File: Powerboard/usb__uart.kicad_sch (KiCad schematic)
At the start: 27 parts

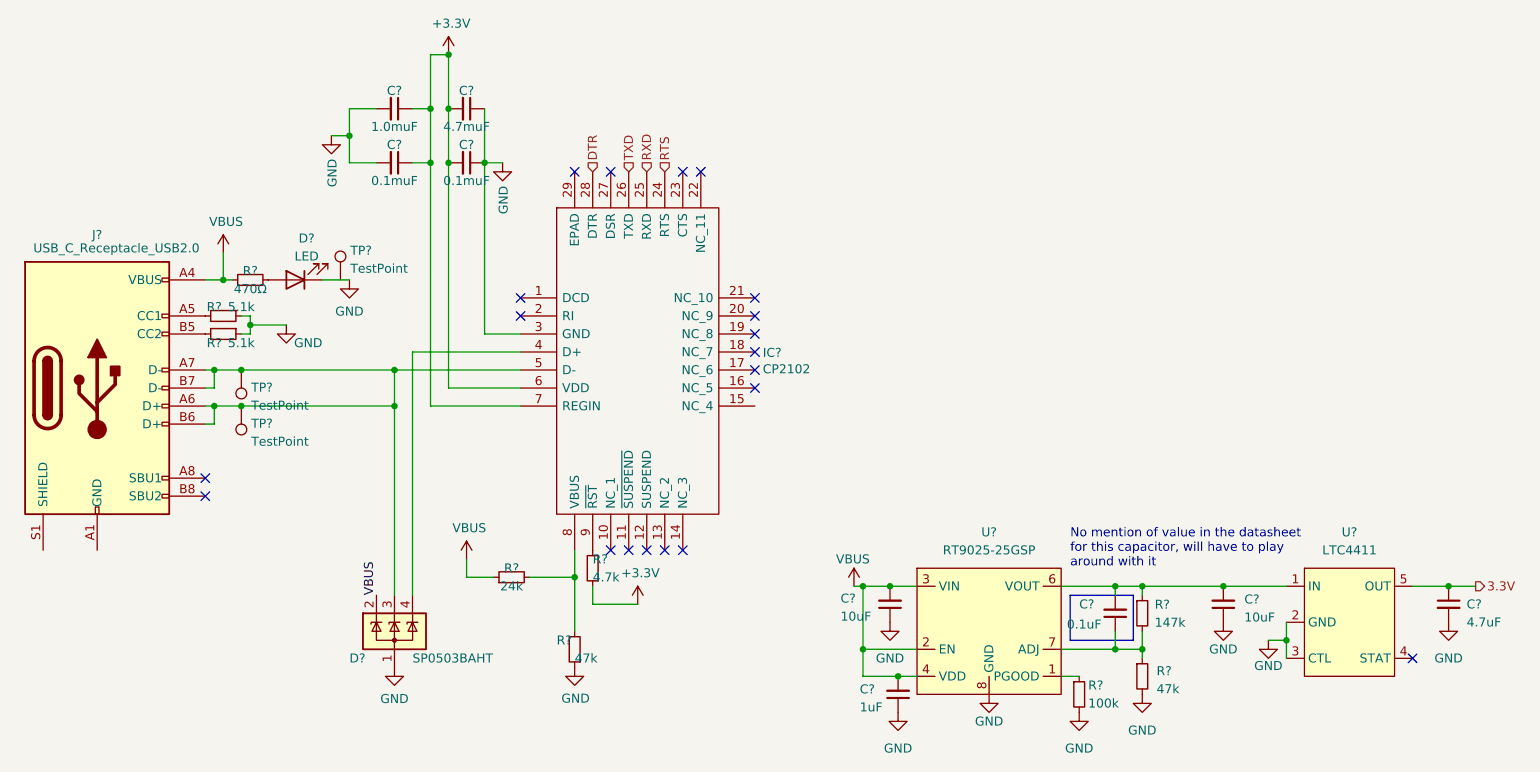
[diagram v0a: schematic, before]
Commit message: removed charger reverse polarity protection
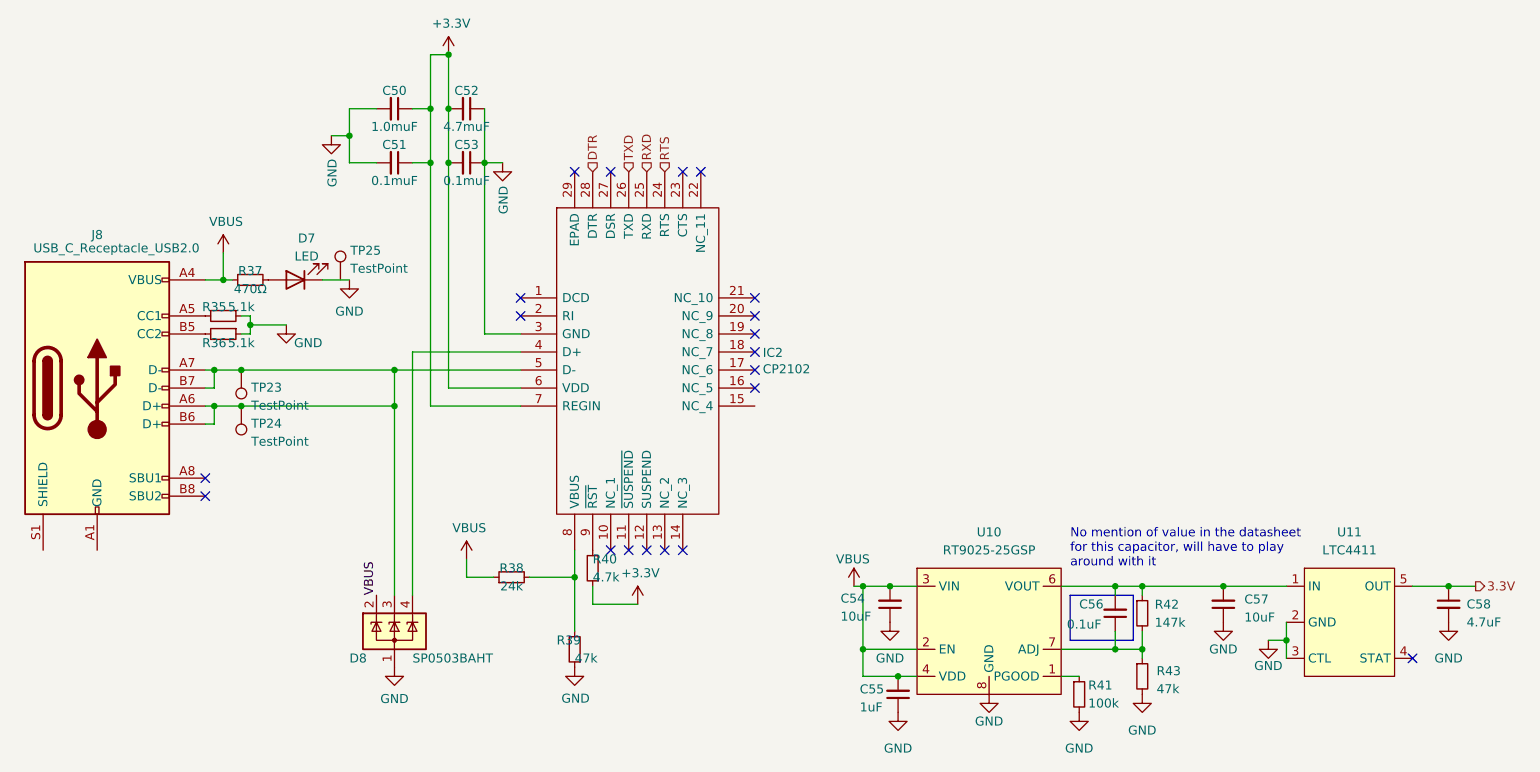
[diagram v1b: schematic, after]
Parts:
- gave numbers to parts that had none: 27

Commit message: changed old mosfets, broke out I2C
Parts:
- removed C55: 1uF, Capacitor_SMD:C_0603_1608Metric, symbol Device:C_Small
- removed C56: 0.1uF, Capacitor_SMD:C_0603_1608Metric, symbol Device:C_Small
- removed R41: 100k, Resistor_SMD:R_0603_1608Metric, symbol Device:R_Small
- R42: value 147k -> 56k
- R43: value 47k -> 10k
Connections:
- net VBUS: no longer U10.4 (VDD)
- no-connect marks 20 -> 22
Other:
- note removed: "No mention of value in the datasheet for this capacitor, will have to play around with it"
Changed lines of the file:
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@@
   (junction (at 100.33 91.44) (diameter 0) (color 0 0 0 0)
   )
-  (junction (at 223.52 121.92) (diameter 0) (color 0 0 0 0)
-  )
   (junction (at 115.57 58.42) (diameter 0) (color 0 0 0 0)
   )
@@
   (junction (at 100.33 96.52) (diameter 0) (color 0 0 0 0)
   )
-  (junction (at 187.96 130.81) (diameter 0) (color 0 0 0 0)
-  )
   (junction (at 191.77 121.92) (diameter 0) (color 0 0 0 0)
   )
@@
   (junction (at 121.92 96.52) (diameter 0) (color 0 0 0 0)
   )
-  (junction (at 192.9078 134.62) (diameter 0) (color 0 0 0 0)
-  )
   (junction (at 134.62 62.23) (diameter 0) (color 0 0 0 0)
-  )
-  (junction (at 223.52 130.81) (diameter 0) (color 0 0 0 0)
   )
   (junction (at 127 62.23) (diameter 0) (color 0 0 0 0)
@@
   (no_connect (at 147.32 63.5))
   (no_connect (at 95.25 106.68))
+  (no_connect (at 215.9 134.62))
   (no_connect (at 162.56 63.5))
   (no_connect (at 172.72 88.9))
   (no_connect (at 157.48 116.84))
   (no_connect (at 160.02 116.84))
+  (no_connect (at 195.58 134.62))
   (no_connect (at 152.4 116.84))
   (no_connect (at 172.72 93.98))
@@
     (stroke (width 0) (type default) (color 0 0 0 0))
   )
-  (polyline (pts (xy 217.17 129.54) (xy 226.06 129.54))
-    (stroke (width 0) (type default) (color 0 0 0 0))
-  )
   (wire (pts (xy 191.77 121.92) (xy 195.58 121.92))
     (stroke (width 0) (type default) (color 0 0 0 0))
@@
     (stroke (width 0) (type default) (color 0 0 0 0))
   )
-  (polyline (pts (xy 226.06 129.54) (xy 226.06 123.19))
-    (stroke (width 0) (type default) (color 0 0 0 0))
-  )
   (wire (pts (xy 127 46.99) (xy 129.54 46.99))
     (stroke (width 0) (type default) (color 0 0 0 0))
@@
     (stroke (width 0) (type default) (color 0 0 0 0))
   )
-  (wire (pts (xy 223.52 130.81) (xy 227.33 130.81))
+  (wire (pts (xy 215.9 130.81) (xy 227.33 130.81))
     (stroke (width 0) (type default) (color 0 0 0 0))
   )
@@
     (stroke (width 0) (type default) (color 0 0 0 0))
   )
-  (wire (pts (xy 187.96 130.81) (xy 187.96 134.62))
-    (stroke (width 0) (type default) (color 0 0 0 0))
-  )
   (wire (pts (xy 227.33 128.27) (xy 227.33 130.81))
     (stroke (width 0) (type default) (color 0 0 0 0))
@@
     (stroke (width 0) (type default) (color 0 0 0 0))
   )
-  (polyline (pts (xy 217.17 123.19) (xy 217.17 129.54))
-    (stroke (width 0) (type default) (color 0 0 0 0))
-  )
   (wire (pts (xy 96.52 96.52) (xy 96.52 99.06))
     (stroke (width 0) (type default) (color 0 0 0 0))
@@
     (stroke (width 0) (type default) (color 0 0 0 0))
   )
-  (wire (pts (xy 187.96 134.62) (xy 192.9078 134.62))
-    (stroke (width 0) (type default) (color 0 0 0 0))
-  )
   (wire (pts (xy 147.32 120.65) (xy 147.32 128.27))
     (stroke (width 0) (type default) (color 0 0 0 0))
@@
     (stroke (width 0) (type default) (color 0 0 0 0))
   )
-  (wire (pts (xy 223.52 121.92) (xy 227.33 121.92))
+  (wire (pts (xy 215.9 121.92) (xy 227.33 121.92))
     (stroke (width 0) (type default) (color 0 0 0 0))
   )
@@
     (stroke (width 0) (type default) (color 0 0 0 0))
   )
-  (wire (pts (xy 192.9078 134.62) (xy 195.58 134.62))
-    (stroke (width 0) (type default) (color 0 0 0 0))
-  )
   (wire (pts (xy 95.25 96.52) (xy 96.52 96.52))
     (stroke (width 0) (type default) (color 0 0 0 0))
   )
-  (wire (pts (xy 215.9 130.81) (xy 223.52 130.81))
-    (stroke (width 0) (type default) (color 0 0 0 0))
-  )
   (wire (pts (xy 121.92 91.44) (xy 139.7 91.44))
     (stroke (width 0) (type default) (color 0 0 0 0))
   )
-  (wire (pts (xy 223.52 128.27) (xy 223.52 130.81))
-    (stroke (width 0) (type default) (color 0 0 0 0))
-  )
   (wire (pts (xy 115.57 58.42) (xy 115.57 62.23))
     (stroke (width 0) (type default) (color 0 0 0 0))
   )
-  (wire (pts (xy 215.9 134.62) (xy 218.44 134.62))
-    (stroke (width 0) (type default) (color 0 0 0 0))
-  )
   (wire (pts (xy 149.86 121.92) (xy 149.86 124.46))
     (stroke (width 0) (type default) (color 0 0 0 0))
   )
-  (wire (pts (xy 215.9 121.92) (xy 223.52 121.92))
-    (stroke (width 0) (type default) (color 0 0 0 0))
-  )
   (wire (pts (xy 97.79 74.93) (xy 97.79 78.74))
     (stroke (width 0) (type default) (color 0 0 0 0))
@@
     (stroke (width 0) (type default) (color 0 0 0 0))
   )
-  (polyline (pts (xy 217.17 123.19) (xy 226.06 123.19))
-    (stroke (width 0) (type default) (color 0 0 0 0))
-  )
   (wire (pts (xy 127 62.23) (xy 124.46 62.23))
     (stroke (width 0) (type default) (color 0 0 0 0))
@@
   (wire (pts (xy 95.25 91.44) (xy 96.52 91.44))
     (stroke (width 0) (type default) (color 0 0 0 0))
-  )
-  (wire (pts (xy 223.52 121.92) (xy 223.52 123.19))
-    (stroke (width 0) (type default) (color 0 0 0 0))
-  )
-  (text "No mention of value in the datasheet \nfor this capacitor, will have to play\naround with it\n"
-    (at 217.17 119.38 0)
-    (effects (font (size 1.27 1.27)) (justify left bottom))
   )
   (label "VBUS" (at 119.38 123.19 90)
@@
     )
     (property "Datasheet" "~" (id 3) (at 191.77 124.46 0)
-      (effects (font (size 1.27 1.27)) hide)
-    )
-    (pin "1")
-    (pin "2")
-  )
-  (symbol (lib_id "Device:R_Small") (at 218.44 137.16 0) (unit 1)
-    (in_bom yes) (on_board yes)
-    (property "Reference" "R41" (id 0) (at 219.71 135.89 0)
-      (effects (font (size 1.27 1.27)) (justify left))
-    )
-    (property "Value" "100k" (id 1) (at 219.71 138.43 0)
-      (effects (font (size 1.27 1.27)) (justify left))
-    )
-    (property "Footprint" "Resistor_SMD:R_0603_1608Metric" (id 2) (at 218.44 137.16 0)
-      (effects (font (size 1.27 1.27)) hide)
-    )
-    (property "Datasheet" "~" (id 3) (at 218.44 137.16 0)
       (effects (font (size 1.27 1.27)) hide)
     )
@@
       (effects (font (size 1.27 1.27)) (justify left))
     )
-    (property "Value" "47k" (id 1) (at 229.344 136.4097 0)
+    (property "Value" "10k" (id 1) (at 229.344 136.4097 0)
       (effects (font (size 1.27 1.27)) (justify left))
     )
@@
     )
     (property "Datasheet" "~" (id 3) (at 227.33 134.62 0)
-      (effects (font (size 1.27 1.27)) hide)
-    )
-    (pin "1")
-    (pin "2")
-  )
-  (symbol (lib_id "Device:C_Small") (at 223.52 125.73 180) (unit 1)
-    (in_bom yes) (on_board yes)
-    (property "Reference" "C56" (id 0) (at 218.44 124.46 0)
-      (effects (font (size 1.27 1.27)) (justify right))
-    )
-    (property "Value" "0.1uF" (id 1) (at 216.6997 127.2978 0)
-      (effects (font (size 1.27 1.27)) (justify right))
-    )
-    (property "Footprint" "Capacitor_SMD:C_0603_1608Metric" (id 2) (at 223.52 125.73 0)
-      (effects (font (size 1.27 1.27)) hide)
-    )
-    (property "Datasheet" "~" (id 3) (at 223.52 125.73 0)
       (effects (font (size 1.27 1.27)) hide)
     )
@@
     (pin "1")
   )
-  (symbol (lib_id "Device:C_Small") (at 192.9078 137.16 180) (unit 1)
-    (in_bom yes) (on_board yes)
-    (property "Reference" "C55" (id 0) (at 187.5046 136.4362 0)
-      (effects (font (size 1.27 1.27)) (justify right))
-    )
-    (property "Value" "1uF" (id 1) (at 187.5046 138.9762 0)
-      (effects (font (size 1.27 1.27)) (justify right))
-    )
-    (property "Footprint" "Capacitor_SMD:C_0603_1608Metric" (id 2) (at 192.9078 137.16 0)
-      (effects (font (size 1.27 1.27)) hide)
-    )
-    (property "Datasheet" "~" (id 3) (at 192.9078 137.16 0)
-      (effects (font (size 1.27 1.27)) hide)
-    )
-    (pin "1")
-    (pin "2")
-  )
   (symbol (lib_id "power:VBUS") (at 186.69 121.92 0) (unit 1)
     (in_bom yes) (on_board yes)
@@
     (pin "1")
   )
-  (symbol (lib_id "power:GND") (at 192.9078 139.7 0) (unit 1)
-    (in_bom yes) (on_board yes) (fields_autoplaced)
-    (property "Reference" "#PWR0173" (id 0) (at 192.9078 146.05 0)
-      (effects (font (size 1.27 1.27)) hide)
-    )
-    (property "Value" "GND" (id 1) (at 192.9078 144.78 0))
-    (property "Footprint" "" (id 2) (at 192.9078 139.7 0)
-      (effects (font (size 1.27 1.27)) hide)
-    )
-    (property "Datasheet" "" (id 3) (at 192.9078 139.7 0)
-      (effects (font (size 1.27 1.27)) hide)
-    )
-    (pin "1")
-  )
   (symbol (lib_id "Device:R_Small") (at 227.33 125.73 0) (unit 1)
     (in_bom yes) (on_board yes)
@@
       (effects (font (size 1.27 1.27)) (justify left))
     )
-    (property "Value" "147k" (id 1) (at 229.0867 127.0405 0)
+    (property "Value" "56k" (id 1) (at 229.0867 127.0405 0)
       (effects (font (size 1.27 1.27)) (justify left))
     )
@@
       (effects (font (size 1.27 1.27)) hide)
     )
-    (pin "1")
-  )
-  (symbol (lib_id "power:GND") (at 218.44 139.7 0) (unit 1)
-    (in_bom yes) (on_board yes) (fields_autoplaced)
-    (property "Reference" "#PWR0172" (id 0) (at 218.44 146.05 0)
-      (effects (font (size 1.27 1.27)) hide)
-    )
-    (property "Value" "GND" (id 1) (at 218.44 144.78 0))
-    (property "Footprint" "" (id 2) (at 218.44 139.7 0)
-      (effects (font (size 1.27 1.27)) hide)
-    )
-    (property "Datasheet" "" (id 3) (at 218.44 139.7 0)
-      (effects (font (size 1.27 1.27)) hide)
-    )

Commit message: 3v3 reg cap & inductor changes, added boost capacitor
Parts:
- D7: footprint (none) -> LED_SMD:LED_0603_1608Metric
- J8: footprint (none) -> Connector_USB:USB_C_Receptacle_GCT_USB4085
- TP23, TP24, TP25: footprint (none) -> TestPoint:TestPoint_Pad_D1.0mm
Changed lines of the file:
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@@
     (property "Reference" "D7" (id 0) (at 109.5375 72.8812 0))
     (property "Value" "LED" (id 1) (at 109.5375 75.4181 0))
-    (property "Footprint" "" (id 2) (at 107.95 78.74 0)
+    (property "Footprint" "LED_SMD:LED_0603_1608Metric" (id 2) (at 107.95 78.74 0)
       (effects (font (size 1.27 1.27)) hide)
     )
@@
       (effects (font (size 1.27 1.27)) (justify right))
     )
-    (property "Footprint" "" (id 2) (at 95.25 91.44 0)
+    (property "Footprint" "TestPoint:TestPoint_Pad_D1.0mm" (id 2) (at 95.25 91.44 0)
       (effects (font (size 1.27 1.27)) hide)
     )
@@
     (property "Reference" "J8" (id 0) (at 80.01 72.39 0))
     (property "Value" "USB_C_Receptacle_USB2.0" (id 1) (at 82.7278 74.2696 0))
-    (property "Footprint" "" (id 2) (at 83.82 93.98 0)
+    (property "Footprint" "Connector_USB:USB_C_Receptacle_GCT_USB4085" (id 2) (at 83.82 93.98 0)
       (effects (font (size 1.27 1.27)) hide)
     )
@@
       (effects (font (size 1.27 1.27)) (justify left))
     )
-    (property "Footprint" "" (id 2) (at 119.38 78.74 0)
+    (property "Footprint" "TestPoint:TestPoint_Pad_D1.0mm" (id 2) (at 119.38 78.74 0)
       (effects (font (size 1.27 1.27)) hide)
     )
@@
       (effects (font (size 1.27 1.27)) (justify right))
     )
-    (property "Footprint" "" (id 2) (at 95.25 96.52 0)
-      (effects (font (size 1.27 1.27)) hide)
-    )
+    (property "Footprint" "TestPoint:TestPoint_Pad_D1.0mm" (id 2) (at 95.25 96.52 0)
+      (effects (font (size 1.27 1.27)) hide)
+    )

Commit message: assigned FPs for ceramic caps & most resistors
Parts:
- IC2: footprint QFN50P500X500X100-29N-D -> (none)
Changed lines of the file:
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@@
       (effects (font (size 1.27 1.27)) (justify left))
     )
-    (property "Footprint" "QFN50P500X500X100-29N-D" (id 2) (at 168.91 68.58 0)
+    (property "Footprint" "" (id 2) (at 168.91 68.58 0)
       (effects (font (size 1.27 1.27)) (justify left) hide)
     )

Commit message: actually changed caps this time
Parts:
- C50, C51, C52, C53: footprint (none) -> Capacitor_SMD:C_0603_1608Metric
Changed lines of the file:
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@@
     (property "Reference" "C50" (id 0) (at 121.92 52.07 90))
     (property "Value" "1.0muF" (id 1) (at 121.92 57.15 90))
-    (property "Footprint" "" (id 2) (at 121.92 54.61 0)
+    (property "Footprint" "Capacitor_SMD:C_0603_1608Metric" (id 2) (at 121.92 54.61 0)
       (effects (font (size 1.27 1.27)) hide)
     )
@@
     (property "Reference" "C53" (id 0) (at 132.08 59.69 90))
     (property "Value" "0.1muF" (id 1) (at 132.08 64.77 90))
-    (property "Footprint" "" (id 2) (at 132.08 62.23 0)
+    (property "Footprint" "Capacitor_SMD:C_0603_1608Metric" (id 2) (at 132.08 62.23 0)
       (effects (font (size 1.27 1.27)) hide)
     )
@@
     (property "Reference" "C51" (id 0) (at 121.92 59.69 90))
     (property "Value" "0.1muF" (id 1) (at 121.92 64.77 90))
-    (property "Footprint" "" (id 2) (at 121.92 62.23 0)
+    (property "Footprint" "Capacitor_SMD:C_0603_1608Metric" (id 2) (at 121.92 62.23 0)
       (effects (font (size 1.27 1.27)) hide)
     )
@@
     (property "Reference" "C52" (id 0) (at 132.08 52.07 90))
     (property "Value" "4.7muF" (id 1) (at 132.08 57.15 90))
-    (property "Footprint" "" (id 2) (at 132.08 54.61 0)
+    (property "Footprint" "Capacitor_SMD:C_0603_1608Metric" (id 2) (at 132.08 54.61 0)
       (effects (font (size 1.27 1.27)) hide)
     )

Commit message: All capacitors selected, most other footprints assigned
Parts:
- C54, C57: footprint Capacitor_SMD:C_0603_1608Metric -> Capacitor_SMD:C_0805_2012Metric
- IC2: footprint (none) -> iclr:QFN28G_0.5-5X5MM
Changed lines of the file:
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@@
       (effects (font (size 1.27 1.27)) (justify right))
     )
-    (property "Footprint" "Capacitor_SMD:C_0603_1608Metric" (id 2) (at 191.77 124.46 0)
+    (property "Footprint" "Capacitor_SMD:C_0805_2012Metric" (id 2) (at 191.77 124.46 0)
       (effects (font (size 1.27 1.27)) hide)
     )
@@
       (effects (font (size 1.27 1.27)) (justify right))
     )
-    (property "Footprint" "Capacitor_SMD:C_0603_1608Metric" (id 2) (at 238.76 124.46 0)
+    (property "Footprint" "Capacitor_SMD:C_0805_2012Metric" (id 2) (at 238.76 124.46 0)
       (effects (font (size 1.27 1.27)) hide)
     )
@@
       (effects (font (size 1.27 1.27)) (justify left))
     )
-    (property "Footprint" "" (id 2) (at 168.91 68.58 0)
+    (property "Footprint" "iclr:QFN28G_0.5-5X5MM" (id 2) (at 168.91 68.58 0)
       (effects (font (size 1.27 1.27)) (justify left) hide)
     )

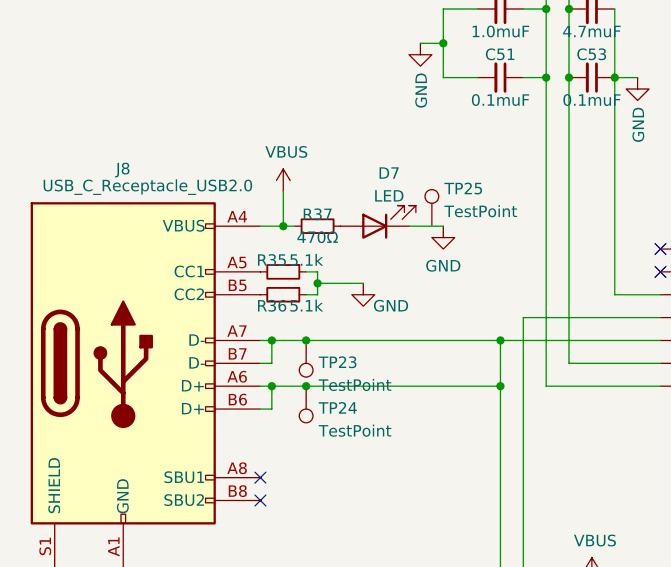
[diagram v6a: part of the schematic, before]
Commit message: Finished footprint assignment
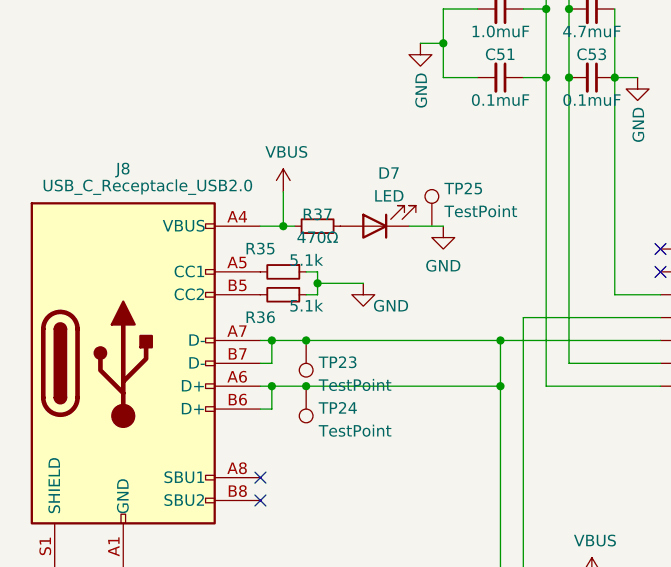
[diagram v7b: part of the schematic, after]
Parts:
- R35, R36, R37, R38, R39, R40: footprint (none) -> Resistor_SMD:R_0603_1608Metric
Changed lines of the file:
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@@
       (effects (font (size 1.27 1.27)) (justify right))
     )
-    (property "Footprint" "" (id 2) (at 147.32 130.81 0)
+    (property "Footprint" "Resistor_SMD:R_0603_1608Metric" (id 2) (at 147.32 130.81 0)
       (effects (font (size 1.27 1.27)) hide)
     )
@@
     (property "Reference" "R38" (id 0) (at 138.43 119.38 90))
     (property "Value" "24k" (id 1) (at 138.43 121.92 90))
-    (property "Footprint" "" (id 2) (at 138.43 120.65 0)
+    (property "Footprint" "Resistor_SMD:R_0603_1608Metric" (id 2) (at 138.43 120.65 0)
       (effects (font (size 1.27 1.27)) hide)
     )
@@
     (property "Reference" "R37" (id 0) (at 101.6 77.47 90))
     (property "Value" "470Ω" (id 1) (at 101.6 80.01 90))
-    (property "Footprint" "" (id 2) (at 101.6 78.74 0)
+    (property "Footprint" "Resistor_SMD:R_0603_1608Metric" (id 2) (at 101.6 78.74 0)
       (effects (font (size 1.27 1.27)) hide)
     )
@@
   (symbol (lib_id "Device:R_Small") (at 97.79 83.82 270) (unit 1)
     (in_bom yes) (on_board yes)
-    (property "Reference" "R35" (id 0) (at 96.52 82.55 90))
+    (property "Reference" "R35" (id 0) (at 95.25 81.28 90))
     (property "Value" "5.1k" (id 1) (at 100.33 82.55 90))
-    (property "Footprint" "" (id 2) (at 97.79 83.82 0)
+    (property "Footprint" "Resistor_SMD:R_0603_1608Metric" (id 2) (at 97.79 83.82 0)
       (effects (font (size 1.27 1.27)) hide)
     )
@@
   (symbol (lib_id "Device:R_Small") (at 97.79 86.36 270) (unit 1)
     (in_bom yes) (on_board yes)
-    (property "Reference" "R36" (id 0) (at 96.52 87.63 90))
+    (property "Reference" "R36" (id 0) (at 95.25 88.9 90))
     (property "Value" "5.1k" (id 1) (at 100.33 87.63 90))
-    (property "Footprint" "" (id 2) (at 97.79 86.36 0)
+    (property "Footprint" "Resistor_SMD:R_0603_1608Metric" (id 2) (at 97.79 86.36 0)
       (effects (font (size 1.27 1.27)) hide)
     )
@@
       (effects (font (size 1.27 1.27)) (justify right))
     )
-    (property "Footprint" "" (id 2) (at 149.86 119.38 0)
-      (effects (font (size 1.27 1.27)) hide)
-    )
+    (property "Footprint" "Resistor_SMD:R_0603_1608Metric" (id 2) (at 149.86 119.38 0)
+      (effects (font (size 1.27 1.27)) hide)
+    )
